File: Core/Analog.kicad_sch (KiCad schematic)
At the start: 41 parts, among them J10 AudioJack3_SwitchTR, J7 AudioJack3_SwitchTR, J8 AudioJack3_SwitchTR, J9 AudioJack3_SwitchTR, U4 TL072, U6 ES9023P, U7 PCM1808, U8 TL072

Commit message: Minor fixes
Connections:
- net at R13.1, U4.3 (+): now also U6.8 (AOUTR); no longer U6.7 (AOUTL)
- net at R12.1, U4.5 (+): now also U6.7 (AOUTL); no longer U6.8 (AOUTR)
- net at R22.1: now also J10.T; no longer J9.T
- net at R24.1: now also J9.T; no longer J10.T
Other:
- moved on the sheet: J10, J7, J8, J9, R14, R15, R16, R17, R20, R21, U4A, U4B

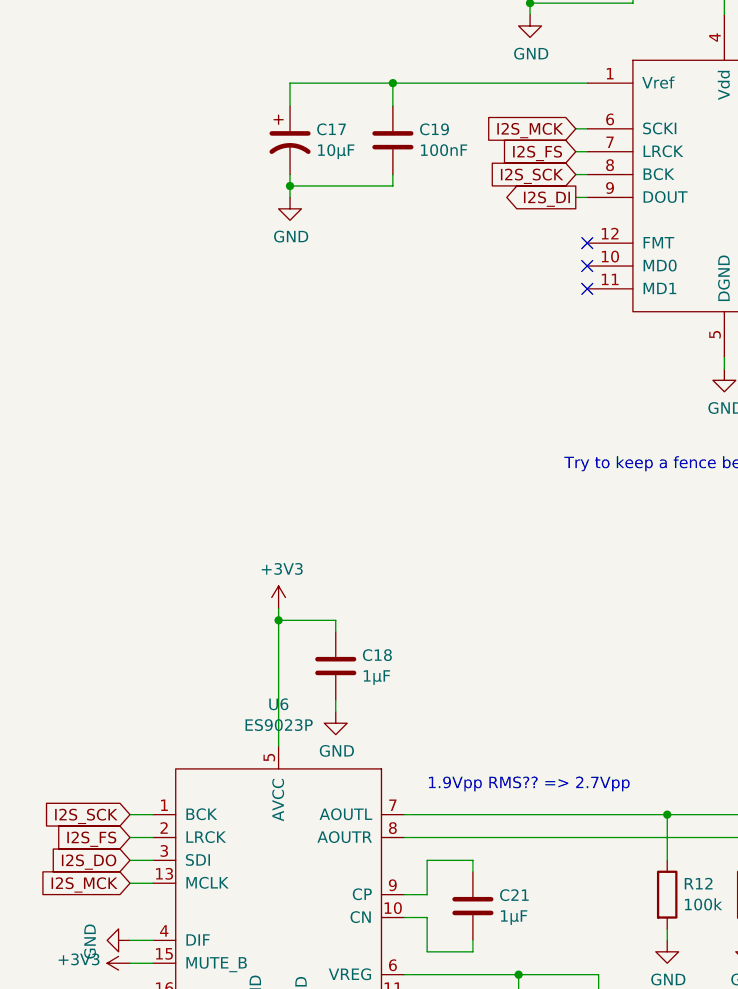
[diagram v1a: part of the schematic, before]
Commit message: Switch to RP2040
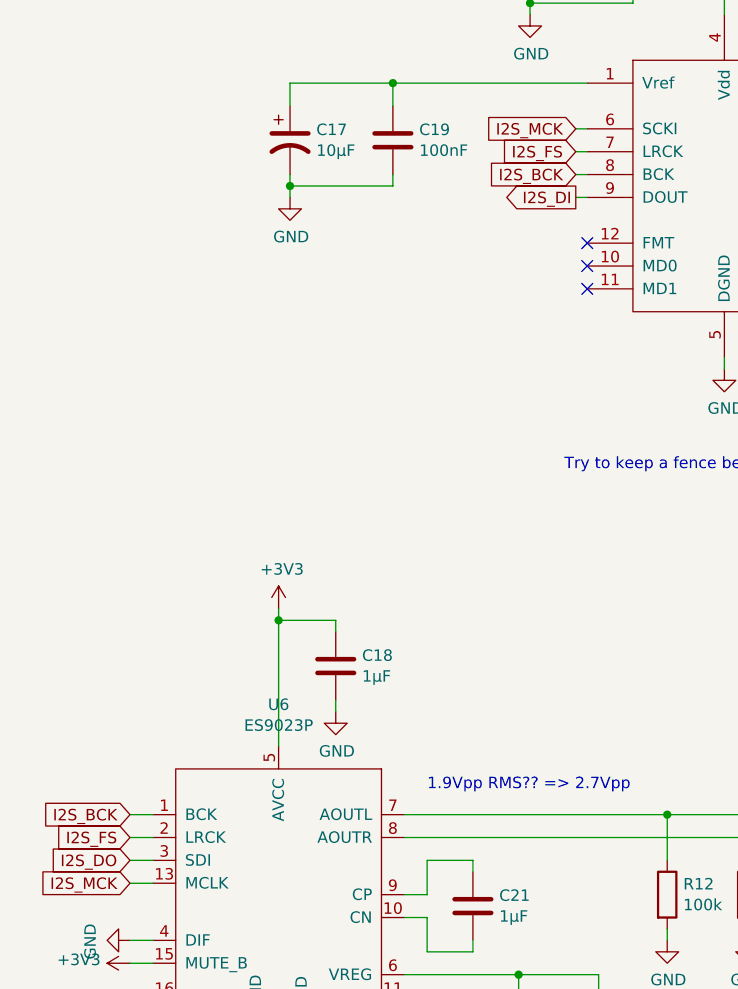
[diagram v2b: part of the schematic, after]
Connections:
- net I2S_SCK renamed I2S_BCK
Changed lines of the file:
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@@
     )
   )
-  (global_label "I2S_SCK" (shape input) (at 121.92 68.58 180)
+  (global_label "I2S_BCK" (shape input) (at 121.92 68.58 180)
     (effects (font (size 1.27 1.27)) (justify right))
     (property "Intersheetrefs" "${INTERSHEET_REFS}" (at 121.92 68.58 0)
@@
     )
   )
-  (global_label "I2S_SCK" (shape input) (at 72.39 139.7 180)
+  (global_label "I2S_BCK" (shape input) (at 72.39 139.7 180)
     (effects (font (size 1.27 1.27)) (justify right))
     (property "Intersheetrefs" "${INTERSHEET_REFS}" (at 72.39 139.7 0)

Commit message: Update metadata
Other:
- company: (none) -> GuavTek
- title: (none) -> M2IDI - USB CORE
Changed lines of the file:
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@@
 (kicad_sch (version 20230121) (generator eeschema)
   (paper "A4")
+  (title_block
+    (title "M2IDI - USB CORE")
+    (date "2023-06-18")
+    (rev "2.0")
+    (company "GuavTek")
+  )
   (junction (at 148.59 38.1) (diameter 0) (color 0 0 0 0)
   )

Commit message: Add optional solder bridge++
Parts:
- added NT1: NetTie_2, Jumper:SolderJumper-2_P1.3mm_Open_RoundedPad1.0x1.5mm, symbol Device:NetTie_2
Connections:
- net at J8.R: now also NT1.2
- net at J7.TN: now also NT1.1
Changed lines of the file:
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@@
+    (stroke (width 0) (type default))
+  )
+  (wire (pts (xy 196.85 120.65) (xy 196.85 152.4))
     (stroke (width 0) (type default))
   )
@@
     (stroke (width 0) (type default))
   )
+  (wire (pts (xy 203.2 152.4) (xy 205.74 152.4))
+    (stroke (width 0) (type default))
+  )
   (wire (pts (xy 181.61 55.88) (xy 181.61 57.15))
     (stroke (width 0) (type default))
@@
     (stroke (width 0) (type default))
   )
+  (wire (pts (xy 196.85 152.4) (xy 198.12 152.4))
+    (stroke (width 0) (type default))
+  )
   (wire (pts (xy 208.28 30.48) (xy 209.55 30.48))
     (stroke (width 0) (type default))
@@
   )
   (wire (pts (xy 123.19 63.5) (xy 121.92 63.5))
+    (stroke (width 0) (type default))
+  )
+  (wire (pts (xy 203.2 120.65) (xy 196.85 120.65))
     (stroke (width 0) (type default))
   )
@@
         )
       )
+    )
+  )
+  (symbol (lib_id "Device:NetTie_2") (at 200.66 152.4 180) (unit 1)
+    (in_bom no) (on_board yes) (dnp no)
+    (property "Reference" "NT1" (at 200.66 155.575 0)
+      (effects (font (size 1.27 1.27)))
+    )
+    (property "Value" "NetTie_2" (at 200.66 153.67 0)
+      (effects (font (size 1.27 1.27)))
+    )
+    (property "Footprint" "Jumper:SolderJumper-2_P1.3mm_Open_RoundedPad1.0x1.5mm" (at 200.66 152.4 0)
+      (effects (font (size 1.27 1.27)) hide)
+    )
+    (property "Datasheet" "~" (at 200.66 152.4 0)
+      (effects (font (size 1.27 1.27)) hide)
+    )
+    (pin "1")
+    (pin "2")
+    (instances
+      (project "MIDI_USB"
+        (path "/cd312ada-837c-497f-a52a-4441719dc9d4/00000000-0000-0000-0000-000060a3eecb"
+          (reference "NT1") (unit 1)
+        )
+      )
